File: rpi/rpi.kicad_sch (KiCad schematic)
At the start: 2 parts, among them J1 Raspberry_Pi_2_3, U1 Ai-Thinker-Ra-02

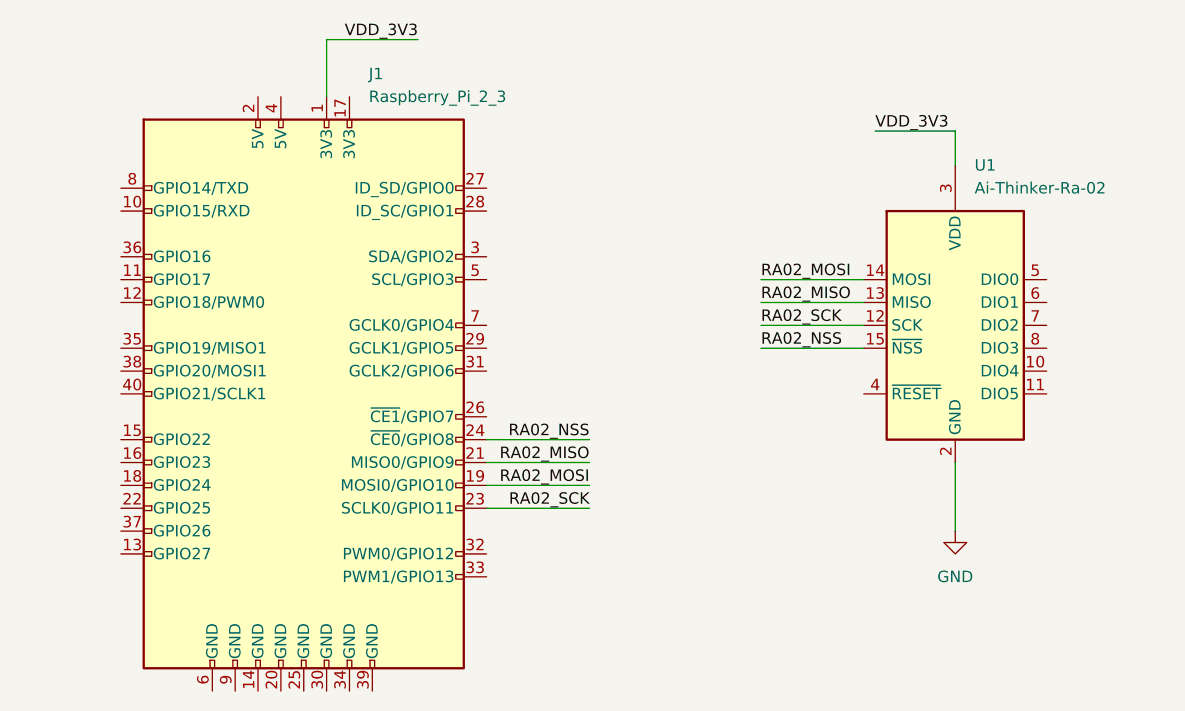
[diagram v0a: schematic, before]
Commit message: feat(rpi): add DIO0 and DIO1 connections
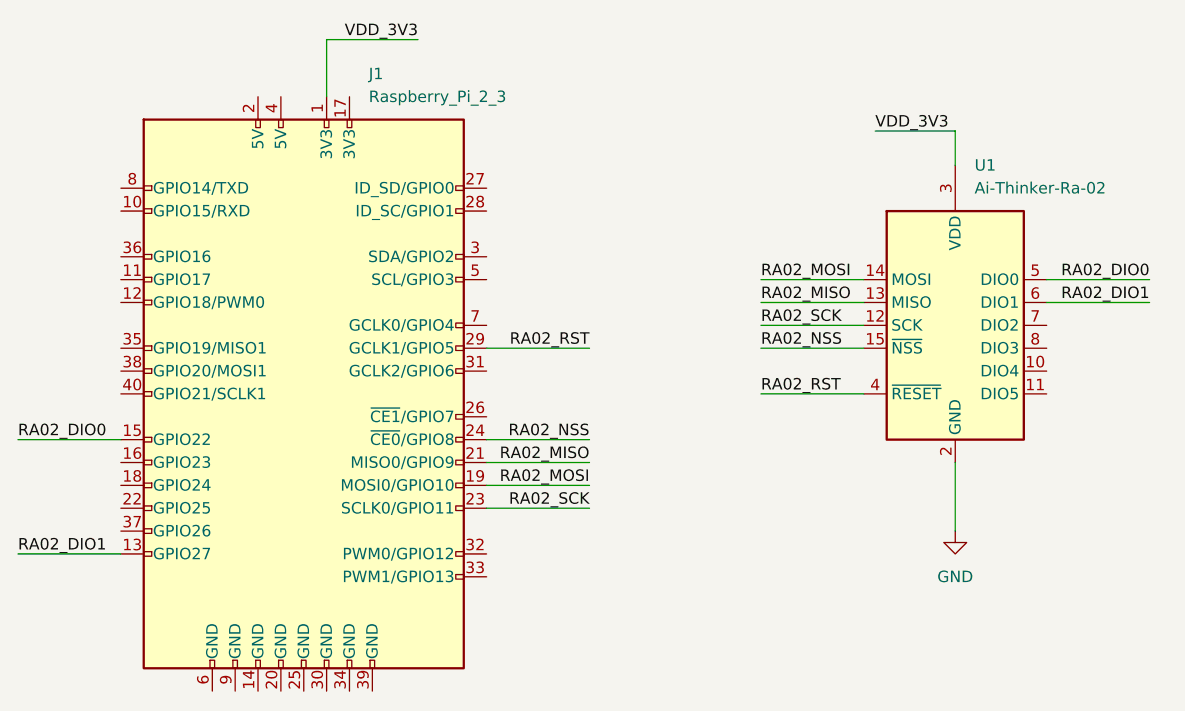
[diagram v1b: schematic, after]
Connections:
- net RA02_RST: now reaches U1.4 (~{RESET})
- net RA02_RST: now also J1.29 (GCLK1/GPIO5)
- net RA02_DIO0: now reaches U1.5 (DIO0)
- net RA02_DIO0: now also J1.15 (GPIO22)
- net RA02_DIO1: now reaches U1.6 (DIO1)
- net RA02_DIO1: now also J1.13 (GPIO27)
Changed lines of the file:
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@@
+	(wire
+		(pts
+			(xy 172.72 77.47) (xy 184.15 77.47)
+		)
+		(stroke
+			(width 0)
+			(type default)
+		)
+	)
 	(wire
 		(pts
@@
 	(wire
 		(pts
+			(xy 204.47 67.31) (xy 215.9 67.31)
+		)
+		(stroke
+			(width 0)
+			(type default)
+		)
+	)
+	(wire
+		(pts
 			(xy 142.24 90.17) (xy 153.67 90.17)
 		)
@@
 	(wire
 		(pts
+			(xy 204.47 64.77) (xy 215.9 64.77)
+		)
+		(stroke
+			(width 0)
+			(type default)
+		)
+	)
+	(wire
+		(pts
+			(xy 90.17 95.25) (xy 101.6 95.25)
+		)
+		(stroke
+			(width 0)
+			(type default)
+		)
+	)
+	(wire
+		(pts
 			(xy 172.72 69.85) (xy 184.15 69.85)
 		)
@@
 		(pts
 			(xy 142.24 82.55) (xy 153.67 82.55)
+		)
+		(stroke
+			(width 0)
+			(type default)
+		)
+	)
+	(wire
+		(pts
+			(xy 90.17 82.55) (xy 101.6 82.55)
+		)
+		(stroke
+			(width 0)
+			(type default)
+		)
+	)
+	(wire
+		(pts
+			(xy 142.24 72.39) (xy 153.67 72.39)
 		)
 		(stroke
@@
 		)
 	)
+	(label "RA02_DIO0"
+		(at 90.17 82.55 0)
+		(effects
+			(font
+				(size 1.27 1.27)
+			)
+			(justify left bottom)
+		)
+	)
 	(label "RA02_NSS"
 		(at 172.72 72.39 0)
@@
 		)
 	)
+	(label "RA02_DIO1"
+		(at 90.17 95.25 0)
+		(effects
+			(font
+				(size 1.27 1.27)
+			)
+			(justify left bottom)
+		)
+	)
 	(label "RA02_MISO"
 		(at 172.72 67.31 0)
@@
 		)
 	)
+	(label "RA02_RST"
+		(at 172.72 77.47 0)
+		(effects
+			(font
+				(size 1.27 1.27)
+			)
+			(justify left bottom)
+		)
+	)
 	(label "VDD_3V3"
 		(at 185.42 48.26 0)
@@
 		)
 	)
+	(label "RA02_RST"
+		(at 153.67 72.39 180)
+		(effects
+			(font
+				(size 1.27 1.27)
+			)
+			(justify right bottom)
+		)
+	)
 	(label "RA02_NSS"
 		(at 153.67 82.55 180)
@@
 		)
 	)
+	(label "RA02_DIO1"
+		(at 215.9 67.31 180)
+		(effects
+			(font
+				(size 1.27 1.27)
+			)
+			(justify right bottom)
+		)
+	)
 	(label "RA02_SCK"
 		(at 153.67 90.17 180)
@@
 		)
 	)
+	(label "RA02_DIO0"
+		(at 215.9 64.77 180)
+		(effects
+			(font
+				(size 1.27 1.27)
+			)
+			(justify right bottom)
+		)
+	)
